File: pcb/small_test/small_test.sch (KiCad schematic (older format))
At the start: 5 parts, among them U1 ArduinoNano_r3.3

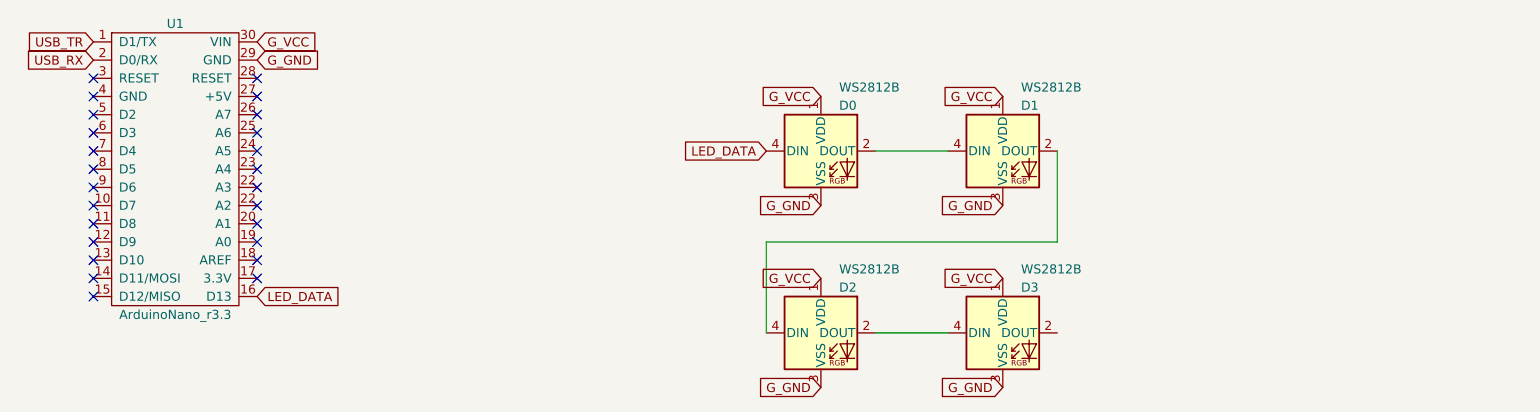
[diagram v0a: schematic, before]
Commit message: Update test PCB with new symbols and added caps
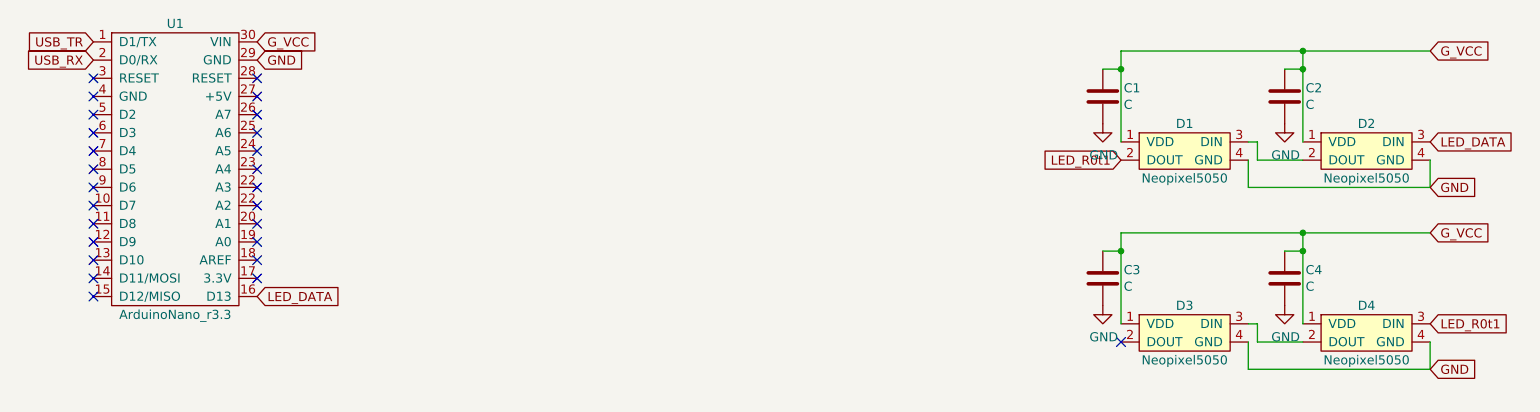
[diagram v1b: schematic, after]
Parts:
- removed D0, D1, D2, D3: WS2812B, LED_SMD:LED_WS2812B_PLCC4_5.0x5.0mm_P3.2mm, symbol LED:WS2812B
- added C1, C2, C3, C4: C, Capacitor_SMD:C_1206_3216Metric_Pad1.42x1.75mm_HandSolder, symbol Device:C
- added D1, D2, D3, D4: Neopixel5050, LED_SMD:LED_WS2812B_PLCC4_5.0x5.0mm_P3.2mm, symbol LED:Neopixel5050
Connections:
- net G_VCC: now also C1.2, C2.2, C3.2, C4.2, D1.1 (VDD), D2.1 (VDD), D3.1 (VDD), D4.1 (VDD)
- net LED_DATA: now also D2.3 (DIN)
- net G_GND renamed GND
- net GND: now also C1.1, C2.1, C3.1, C4.1, D1.4 (GND), D2.4 (GND), D3.4 (GND), D4.4 (GND)
- new net: D1.3 (DIN), D2.2 (DOUT)
- new net: D3.3 (DIN), D4.2 (DOUT)
- new net LED_R0t1: D1.2 (DOUT), D4.3 (DIN)
- no-connect marks 25 -> 26
